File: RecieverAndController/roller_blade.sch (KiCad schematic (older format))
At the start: 1 part

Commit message: did easy stuff
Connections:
- no-connect marks 0 -> 4
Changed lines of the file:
@@
 F6 "PC4" I R 3800 3900 60
 F7 "PC5" I R 3800 4000 60
+F8 "PD0" I L 2400 3450 60
+F9 "PB0" I L 2400 3550 60
 $EndSheet
 $Sheet
@@
 Wire Wire Line
 	5200 2400 5000 2400
+NoConn ~ 2400 3450
+NoConn ~ 2400 3550
+NoConn ~ 3800 3900
+NoConn ~ 3800 4000
 $EndSCHEMATC

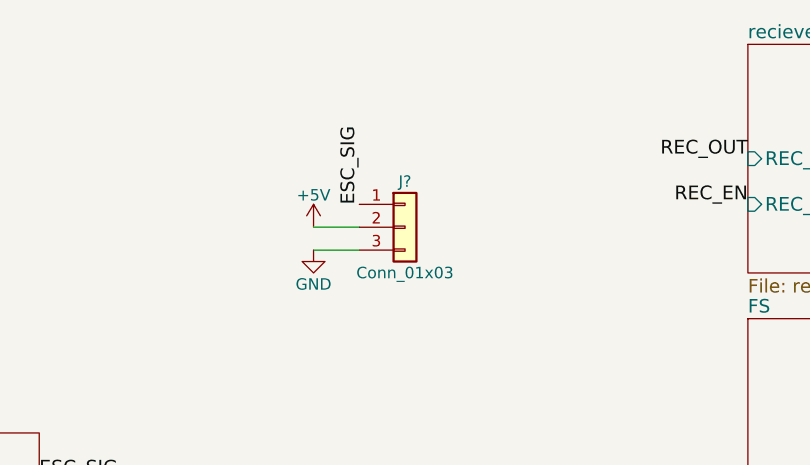
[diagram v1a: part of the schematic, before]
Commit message: adding footprints to schematic
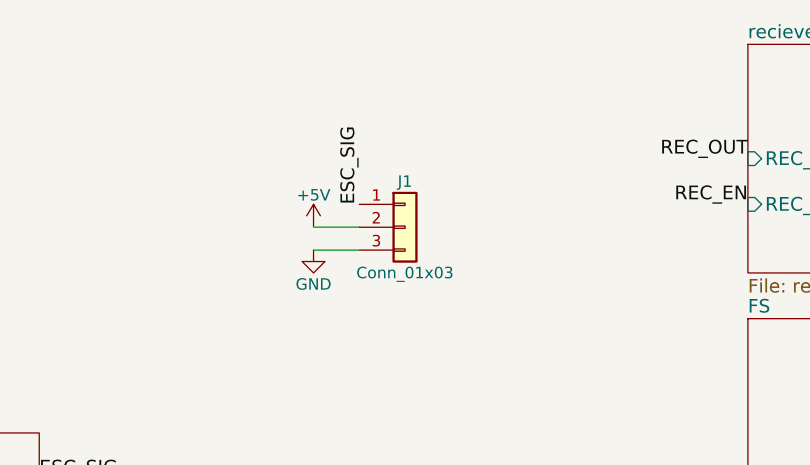
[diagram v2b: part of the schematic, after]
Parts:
- J1: renamed from J?; footprint (none) -> Pin_Headers:Pin_Header_Angled_1x03_Pitch2.54mm
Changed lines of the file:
@@
 $EndSheet
 $Comp
-L GND #PWR?
+L GND #PWR01
 U 1 1 5AC95B6B
 P 5000 2500
-F 0 "#PWR?" H 5000 2250 50  0001 C CNN
+F 0 "#PWR01" H 5000 2250 50  0001 C CNN
 F 1 "GND" H 5000 2350 50  0000 C CNN
 F 2 "" H 5000 2500 50  0001 C CNN
@@
 ENC_OUT
 $Comp
-L Conn_01x03 J?
+L Conn_01x03 J1
 U 1 1 5AC9C77E
 P 5400 2400
-F 0 "J?" H 5400 2600 50  0000 C CNN
+F 0 "J1" H 5400 2600 50  0000 C CNN
 F 1 "Conn_01x03" H 5400 2200 50  0000 C CNN
-F 2 "" H 5400 2400 50  0001 C CNN
+F 2 "Pin_Headers:Pin_Header_Angled_1x03_Pitch2.54mm" H 5400 2400 50  0001 C CNN
 F 3 "" H 5400 2400 50  0001 C CNN
 	1    5400 2400
@@
 $EndComp
 $Comp
-L +5V #PWR?
+L +5V #PWR02
 U 1 1 5AC9C7D9
 P 5000 2400
-F 0 "#PWR?" H 5000 2250 50  0001 C CNN
+F 0 "#PWR02" H 5000 2250 50  0001 C CNN
 F 1 "+5V" H 5000 2540 50  0000 C CNN
 F 2 "" H 5000 2400 50  0001 C CNN
